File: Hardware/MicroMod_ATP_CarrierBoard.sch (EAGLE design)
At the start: 63 parts, among them J19 QWIIC_RIGHT_ANGLE, J2 JTAG, J20 QWIIC_RIGHT_ANGLE, J21 1X04_SMD_STRAIGHT_COMBO, J23 1X04_SMD_STRAIGHT_COMBO, J4 USB_A_SMT_FEMALE, J6 MICROMOD-2222-C, J8 1X04_SMD_STRAIGHT_COMBO, U5 AP7361C-33

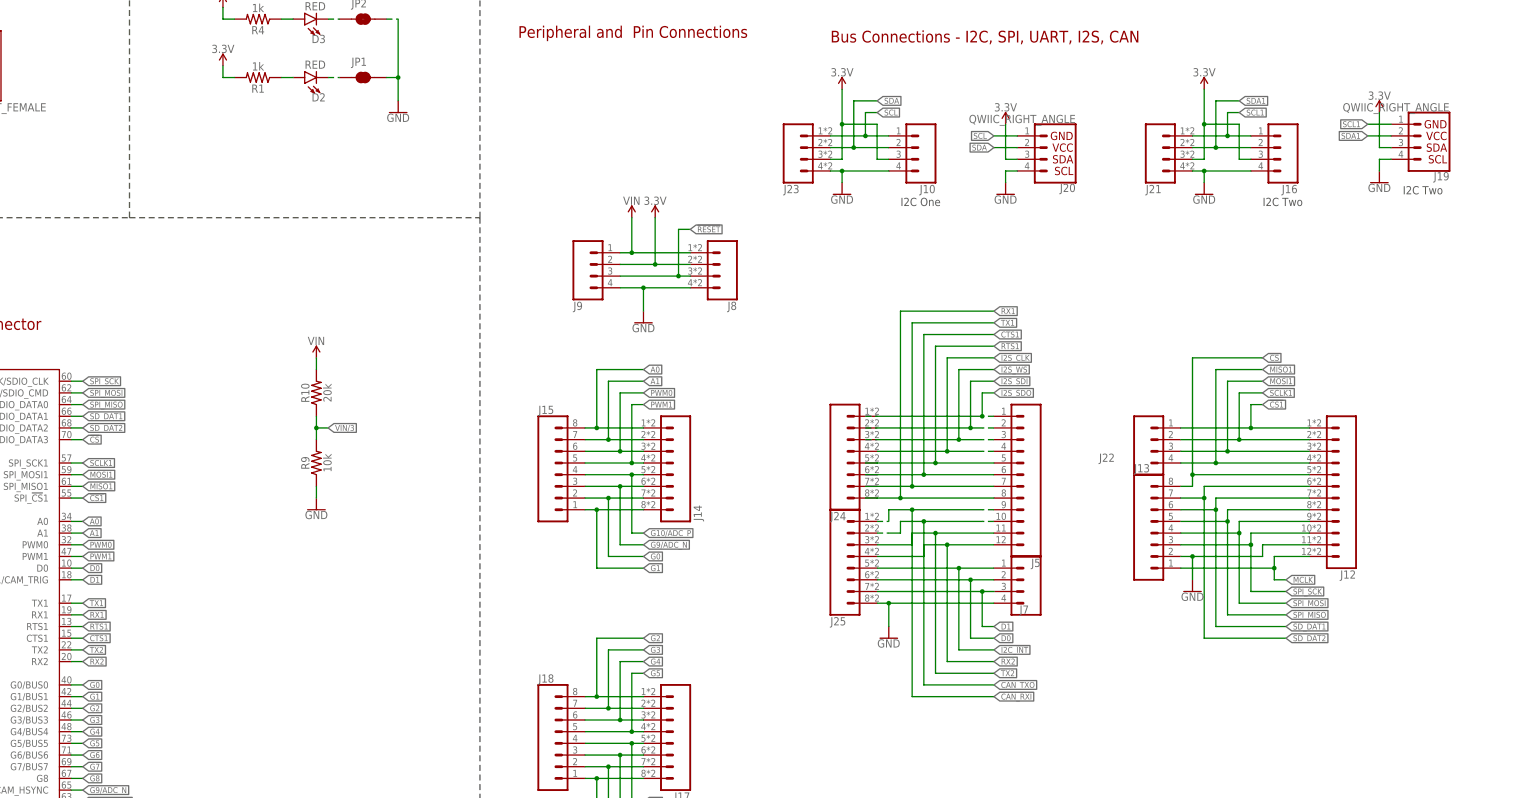
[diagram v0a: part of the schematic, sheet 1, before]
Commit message: Shifts top header assignements to the left to make space for 3v3 and GND pins
* Adds top silk to almost all pins
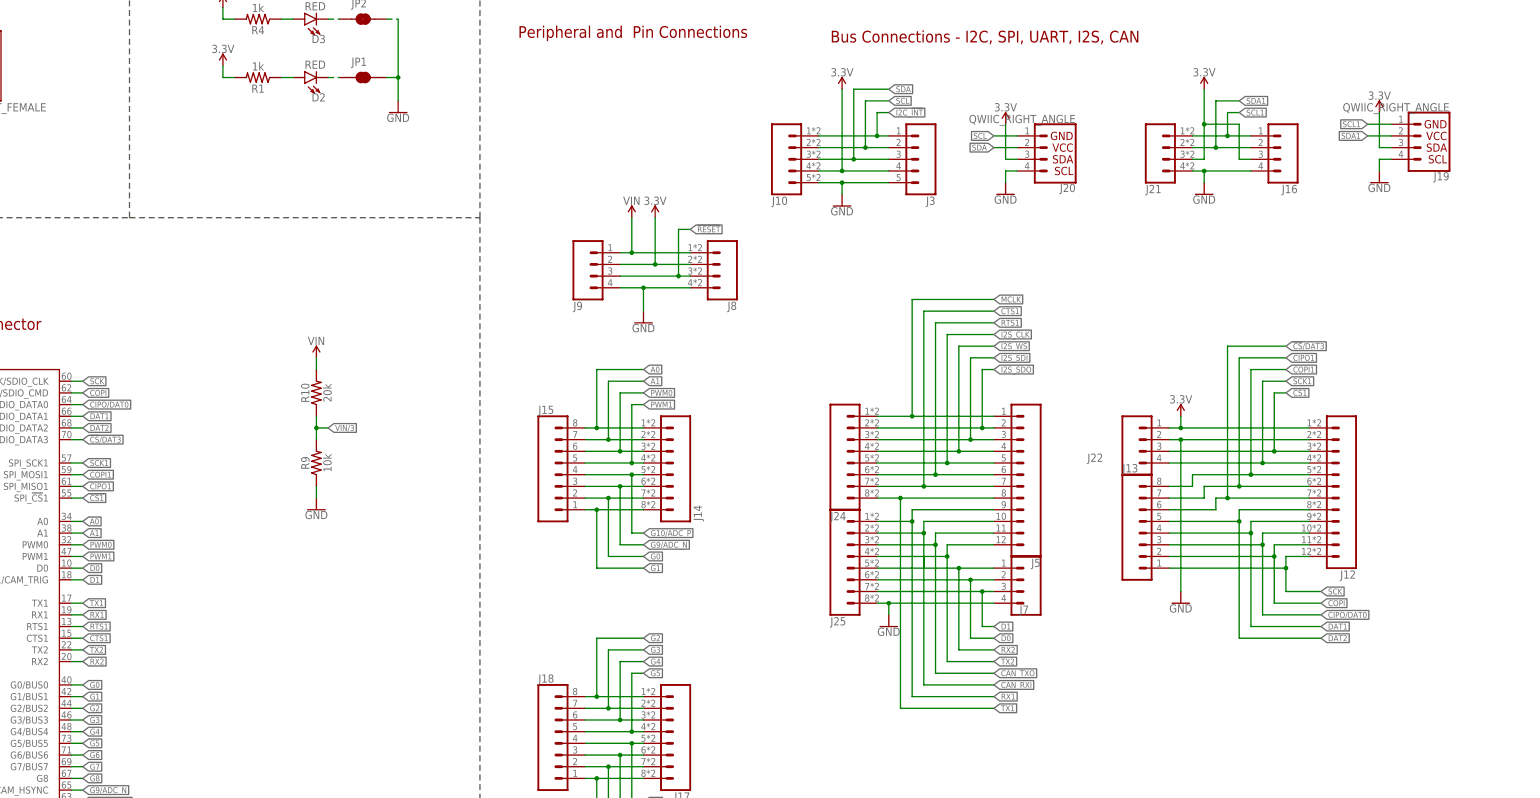
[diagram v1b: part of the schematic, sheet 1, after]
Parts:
- removed J23: 1X04_SMD_STRAIGHT_COMBO, SparkFun-Connectors:CONN_04SMD_STRAIGHT_COMBO
- added J3: (no value), SparkFun-Connectors:CONN_05NO_SILK
- J10: device SparkFun-Connectors:CONN_041X04_NO_SILK_NO_POP -> SparkFun-Connectors:CONN_05VERT_FEMALE_HEADER
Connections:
- removed net !CS!: J12.5, J13.8, J6.SPI_!CS!/SDIO_DATA3
- removed net MISO1: J12.4, J22.4, J6.SPI_MISO1
- removed net MOSI1: J12.3, J22.3, J6.SPI_MOSI1
- removed net SCLK1: J12.2, J22.2, J6.SPI_SCK1
- removed net SD_DAT1: J12.7, J13.6, J6.SDIO_DATA1
- removed net SD_DAT2: J12.6, J13.7, J6.SDIO_DATA2
- removed net SPI_MISO: J12.8, J13.5, J6.SPI_MISO/SDIO_DATA0
- removed net SPI_MOSI: J12.9, J13.4, J6.SPI_MOSI/SDIO_CMD
- removed net SPI_SCK: J12.10, J13.3, J6.SPI_SCK/SDIO_CLK
- new net !CS!/DAT3: J12.7, J13.6, J6.SPI_!CS!/SDIO_DATA3
- new net CIPO/DAT0: J12.10, J13.3, J6.SPI_MISO/SDIO_DATA0
- new net CIPO1: J12.6, J13.7, J6.SPI_MISO1
- new net COPI: J12.11, J13.2, J6.SPI_MOSI/SDIO_CMD
- new net COPI1: J12.5, J13.8, J6.SPI_MOSI1
- new net DAT1: J12.9, J13.4, J6.SDIO_DATA1
- new net DAT2: J12.8, J13.5, J6.SDIO_DATA2
- new net SCK: J12.12, J13.1, J6.SPI_SCK/SDIO_CLK
- new net SCK1: J12.4, J22.4, J6.SPI_SCK1
- net !CS1: now also J12.3, J22.3; no longer J12.1, J22.1
- net 3.3V: now also J10.4, J12.1, J22.1, J3.4; no longer J10.3, J23.3
- net CAN_RXI: now also J25.2, J5.10; no longer J25.1, J5.9
- net CAN_TXO: now also J25.3, J5.11; no longer J25.2, J5.10
- net CTS1: now also J24.7, J5.7; no longer J24.6, J5.6
- net GND: now also J10.5, J12.2, J22.2, J3.5; no longer J10.4, J12.11, J13.2, J23.4
- net I2C_!INT: now also J10.1, J3.1; no longer J25.5, J7.1
- net I2S_CLK: now also J24.5, J5.5; no longer J24.4, J5.4
- net I2S_SDI: now also J24.3, J5.3; no longer J24.2, J5.2
- net I2S_SDO: now also J24.2, J5.2; no longer J24.1, J5.1
- net I2S_WS: now also J24.4, J5.4; no longer J24.3, J5.3
- net MCLK: now also J24.1, J5.1; no longer J12.12, J13.1
- net RTS1: now also J24.6, J5.6; no longer J24.5, J5.5
- net RX1: now also J25.1, J5.9; no longer J24.8, J5.8
- net RX2: now also J25.5, J7.1; no longer J25.4, J5.12
- net SCL: now also J10.2, J3.2; no longer J10.1, J23.1
- net SDA: now also J10.3, J3.3; no longer J10.2, J23.2
- net TX1: now also J24.8, J5.8; no longer J24.7, J5.7
- net TX2: now also J25.4, J5.12; no longer J25.3, J5.11
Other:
- note removed: "I2C One"
- note removed: "I2C Two"
- moved on the sheet: J13, J22

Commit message: Adds the rest of the header labels, fixes or approves DRC errors
* adds Qwiic Mount screw holes
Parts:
- added LOGO1: SFE_LOGO_NAME_FLAME.2_INCH, SparkFun-Aesthetics:SFE_LOGO_NAME_FLAME.2_INCH
- added LOGO2: QWIIC_LOGO_3MM, SparkFun-Aesthetics:QWIIC_LOGO_3MM
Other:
- note added: "Buttons"
- note added: "Headers"
- note added: "LEDs"
- note added: "SWD"
- note added: "Take care when closing this jumper, it removes the 6V/2A fuse."
- note added: "USB Host"
- note added: "v10"
- note removed: "Bus Connections - I2C, SPI, UART, I2S, CAN"
- note removed: "JTAG"
- note removed: "Peripheral and Pin Connections"
- note removed: "This is the penny-in-the-fuse jumper. Close only if you know what you're doing."

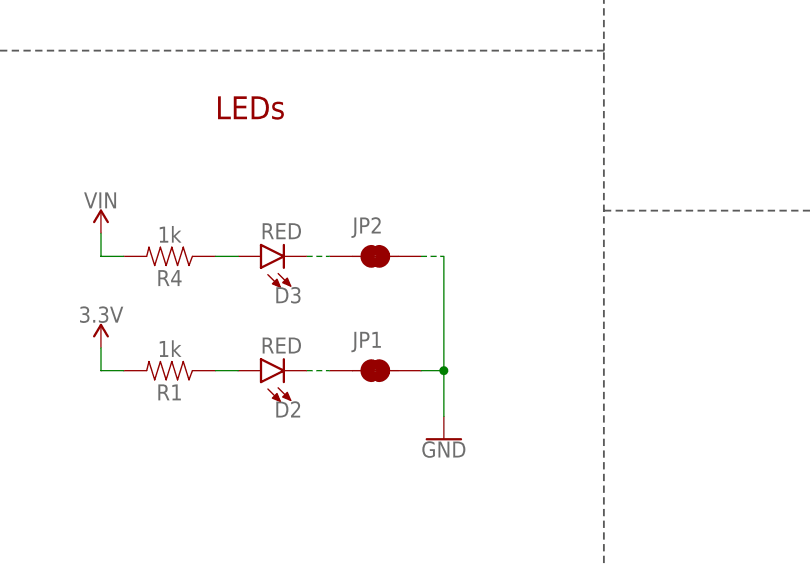
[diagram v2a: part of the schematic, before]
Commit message: Renames LED jumpers to their function
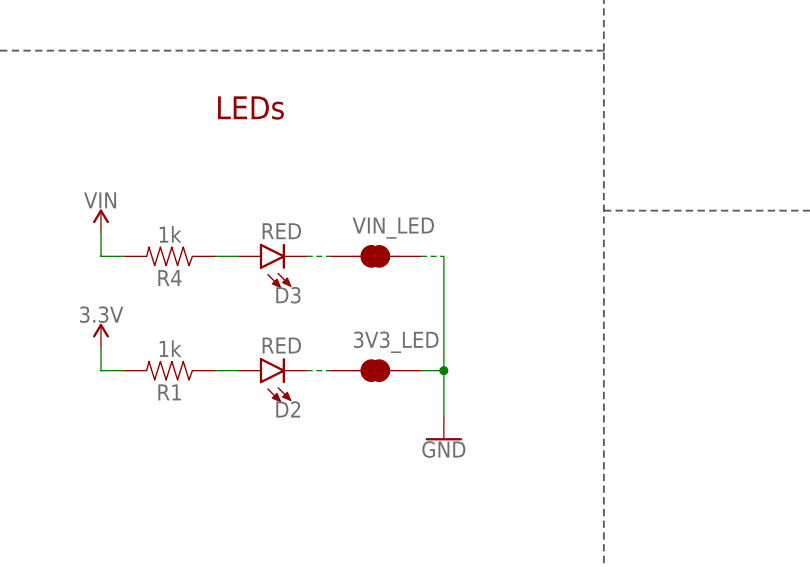
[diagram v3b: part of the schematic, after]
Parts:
- renumbered JP1 to 3V3_LED, JP2 to VIN_LED
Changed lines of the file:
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@@
 <part name="SUPPLY4" library="SparkFun-PowerSymbols" deviceset="VIN" device=""/>
 <part name="SUPPLY7" library="SparkFun-PowerSymbols" deviceset="3.3V" device=""/>
-<part name="JP1" library="SparkFun-Jumpers" deviceset="JUMPER-SMT_2_NC_TRACE" device="_SILK" package3d_urn="urn:adsk.eagle:package:39281/1"/>
-<part name="JP2" library="SparkFun-Jumpers" deviceset="JUMPER-SMT_2_NC_TRACE" device="_SILK" package3d_urn="urn:adsk.eagle:package:39281/1"/>
+<part name="3V3_LED" library="SparkFun-Jumpers" deviceset="JUMPER-SMT_2_NC_TRACE" device="_SILK" package3d_urn="urn:adsk.eagle:package:39281/1"/>
+<part name="VIN_LED" library="SparkFun-Jumpers" deviceset="JUMPER-SMT_2_NC_TRACE" device="_SILK" package3d_urn="urn:adsk.eagle:package:39281/1"/>
 <part name="J3" library="SparkFun-Connectors" deviceset="CONN_05" device="NO_SILK"/>
 <part name="J10" library="SparkFun-Connectors" deviceset="CONN_05" device="VERT_FEMALE_HEADER"/>
@@
 <attribute name="VALUE" x="111.76" y="203.454" size="1.778" layer="96" align="bottom-center"/>
 </instance>
-<instance part="JP1" gate="G$1" x="142.24" y="198.12" smashed="yes">
+<instance part="3V3_LED" gate="G$1" x="142.24" y="198.12" smashed="yes">
 <attribute name="NAME" x="139.7" y="200.66" size="1.778" layer="95" font="vector"/>
 </instance>
-<instance part="JP2" gate="G$1" x="142.24" y="210.82" smashed="yes">
+<instance part="VIN_LED" gate="G$1" x="142.24" y="210.82" smashed="yes">
 <attribute name="NAME" x="139.7" y="213.36" size="1.778" layer="95" font="vector"/>
 </instance>
@@
 </segment>
 <segment>
-<pinref part="JP2" gate="G$1" pin="2"/>
+<pinref part="VIN_LED" gate="G$1" pin="2"/>
 <wire x1="147.32" y1="210.82" x2="149.86" y2="210.82" width="0.1524" layer="91" style="longdash"/>
 <pinref part="GND26" gate="1" pin="GND"/>
 <wire x1="149.86" y1="210.82" x2="149.86" y2="198.12" width="0.1524" layer="91"/>
-<pinref part="JP1" gate="G$1" pin="2"/>
+<pinref part="3V3_LED" gate="G$1" pin="2"/>
 <wire x1="149.86" y1="198.12" x2="149.86" y2="193.04" width="0.1524" layer="91"/>
 <wire x1="147.32" y1="198.12" x2="149.86" y2="198.12" width="0.1524" layer="91"/>
@@
 <segment>
 <pinref part="D2" gate="G$1" pin="C"/>
-<pinref part="JP1" gate="G$1" pin="1"/>
+<pinref part="3V3_LED" gate="G$1" pin="1"/>
 <wire x1="134.62" y1="198.12" x2="137.16" y2="198.12" width="0.1524" layer="91" style="longdash"/>
 </segment>
@@
 <segment>
 <pinref part="D3" gate="G$1" pin="C"/>
-<pinref part="JP2" gate="G$1" pin="1"/>
+<pinref part="VIN_LED" gate="G$1" pin="1"/>
 <wire x1="134.62" y1="210.82" x2="137.16" y2="210.82" width="0.1524" layer="91" style="longdash"/>
 </segment>

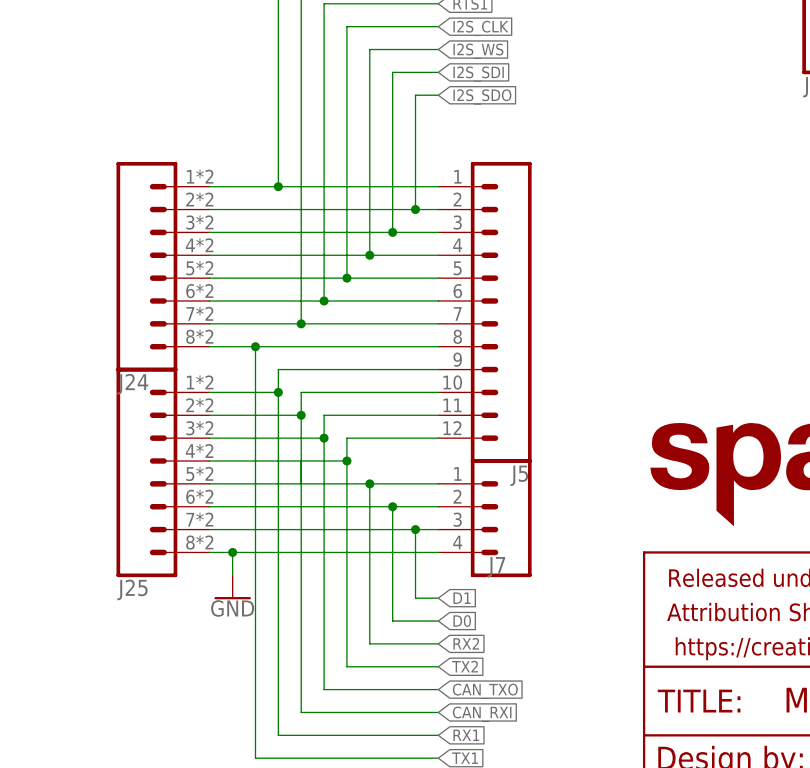
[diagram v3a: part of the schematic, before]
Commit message: Swaps qwiic connectors and their respective headers
* Moves headers on teh top and bottom so that they can be placed properly
* Moves the USB host and USB-C connector down so that labels on teh top can fit
* adjusts the traces accordingly to the part movement
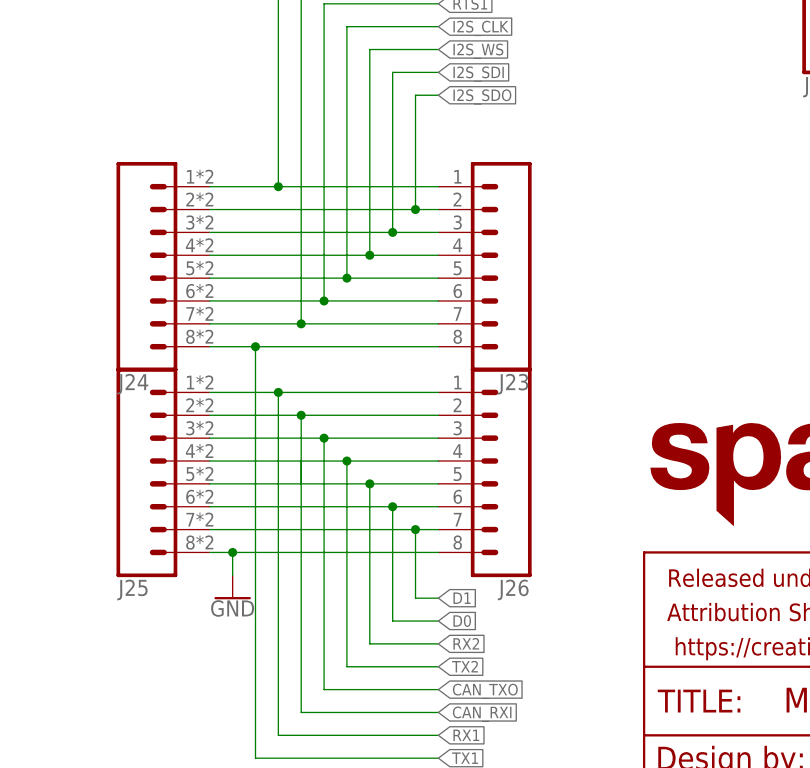
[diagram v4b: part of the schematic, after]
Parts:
- removed J5: (no value), SparkFun-Connectors:CONN_12NO_SILK
- removed J7: (no value), SparkFun-Connectors:CONN_041X04_NO_SILK_NO_POP
- added J23, J26: (no value), SparkFun-Connectors:CONN_08NO_SILK_FEMALE_PTH
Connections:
- net CAN_RXI: now also J26.2; no longer J5.10
- net CAN_TXO: now also J26.3; no longer J5.11
- net CTS1: now also J23.7; no longer J5.7
- net D0: now also J26.6; no longer J7.2
- net D1: now also J26.7; no longer J7.3
- net GND: now also J26.8; no longer J7.4
- net I2S_CLK: now also J23.5; no longer J5.5
- net I2S_SDI: now also J23.3; no longer J5.3
- net I2S_SDO: now also J23.2; no longer J5.2
- net I2S_WS: now also J23.4; no longer J5.4
- net MCLK: now also J23.1; no longer J5.1
- net RTS1: now also J23.6; no longer J5.6
- net RX1: now also J26.1; no longer J5.9
- net RX2: now also J26.5; no longer J7.1
- net TX1: now also J23.8; no longer J5.8
- net TX2: now also J26.4; no longer J5.12

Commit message: Moves GND and 3V3 label on top of board along topside of PCB
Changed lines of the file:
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@@
 </segment>
 <segment>
-<wire x1="287.02" y1="12.7" x2="307.34" y2="12.7" width="0.1524" layer="91"/>
-<label x="307.34" y="12.7" size="1.27" layer="95" xref="yes"/>
-<wire x1="287.02" y1="12.7" x2="287.02" y2="58.42" width="0.1524" layer="91"/>
+<wire x1="287.02" y1="104.14" x2="307.34" y2="104.14" width="0.1524" layer="91"/>
+<label x="307.34" y="104.14" size="1.27" layer="95" xref="yes"/>
+<wire x1="287.02" y1="104.14" x2="287.02" y2="58.42" width="0.1524" layer="91"/>
 <wire x1="307.34" y1="58.42" x2="287.02" y2="58.42" width="0.1524" layer="91"/>
 <pinref part="J24" gate="G$1" pin="8"/>

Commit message: Changes silk labels to bi-directional on G# lines, fixes INPUT/OUTPUT labels on
RTS, CTS, A#, and PWM lines
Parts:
- LOGO1: value SFE_LOGO_NAME_FLAME.2_INCH -> SFE_LOGO_NAME_FLAME.1_INCH; device SparkFun-Aesthetics:SFE_LOGO_NAME_FLAME.2_INCH -> SparkFun-Aesthetics:SFE_LOGO_NAME_FLAME.1_INCH
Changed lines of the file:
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@@
 <part name="J10" library="SparkFun-Connectors" deviceset="CONN_05" device="VERT_FEMALE_HEADER"/>
 <part name="SUPPLY10" library="SparkFun-PowerSymbols" deviceset="3.3V" device=""/>
-<part name="LOGO1" library="SparkFun-Aesthetics" deviceset="SFE_LOGO_NAME_FLAME" device=".2_INCH"/>
 <part name="LOGO2" library="SparkFun-Aesthetics" deviceset="QWIIC_LOGO" device="_3MM"/>
 <part name="J23" library="SparkFun-Connectors" deviceset="CONN_08" device="NO_SILK_FEMALE_PTH"/>
 <part name="J26" library="SparkFun-Connectors" deviceset="CONN_08" device="NO_SILK_FEMALE_PTH"/>
+<part name="LOGO1" library="SparkFun-Aesthetics" deviceset="SFE_LOGO_NAME_FLAME" device=".1_INCH"/>
 </parts>
 <sheets>
@@
 <attribute name="VALUE" x="142.24" y="17.526" size="1.778" layer="96" rot="MR0" align="top-center"/>
 </instance>
-<instance part="LOGO3" gate="G$1" x="411.48" y="45.72" smashed="yes"/>
+<instance part="LOGO3" gate="G$1" x="388.112" y="44.958" smashed="yes"/>
 <instance part="GND19" gate="1" x="55.88" y="10.16" smashed="yes">
 <attribute name="VALUE" x="55.88" y="9.906" size="1.778" layer="96" align="top-center"/>
@@
 <attribute name="VALUE" x="284.48" y="162.814" size="1.778" layer="96" rot="MR0" align="bottom-center"/>
 </instance>
-<instance part="LOGO1" gate="G$1" x="330.2" y="38.1" smashed="yes"/>
-<instance part="LOGO2" gate="G$1" x="388.62" y="38.1" smashed="yes"/>
+<instance part="LOGO2" gate="G$1" x="410.718" y="39.37" smashed="yes"/>
 <instance part="J23" gate="G$1" x="312.42" y="68.58" smashed="yes" rot="R180">
 <attribute name="VALUE" x="317.5" y="81.026" size="1.778" layer="96" font="vector" rot="R180"/>
@@
 <attribute name="NAME" x="317.5" y="32.512" size="1.778" layer="95" font="vector" rot="R180"/>
 </instance>
+<instance part="LOGO1" gate="G$1" x="319.278" y="32.004" smashed="yes"/>
 </instances>
 <busses>
